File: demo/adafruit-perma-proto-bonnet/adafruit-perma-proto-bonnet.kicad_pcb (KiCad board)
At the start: 2 copper layers, 65 x 30 mm, 4 parts

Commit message: Fix bad chars in footprint identifiers
scad can't handle $ in symbol names. This will be a limitation of
the tool
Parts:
- renumbered U$1 to U1, U$3 to U3
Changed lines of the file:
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@@
 		(layer "F.Cu")
 		(at 120.953757 115.515271 -90)
-		(property "Reference" "U$1"
+		(property "Reference" "U1"
 			(at 0 0 -90)
 			(layer "F.SilkS")
@@
 		(at 175.182757 91.555271)
 		(descr "Revision Level Field - 56 mil\n\nSet version with global board attribute '>REV'")
-		(property "Reference" "U$3"
+		(property "Reference" "U3"
 			(at 0 0 0)
 			(layer "F.SilkS")

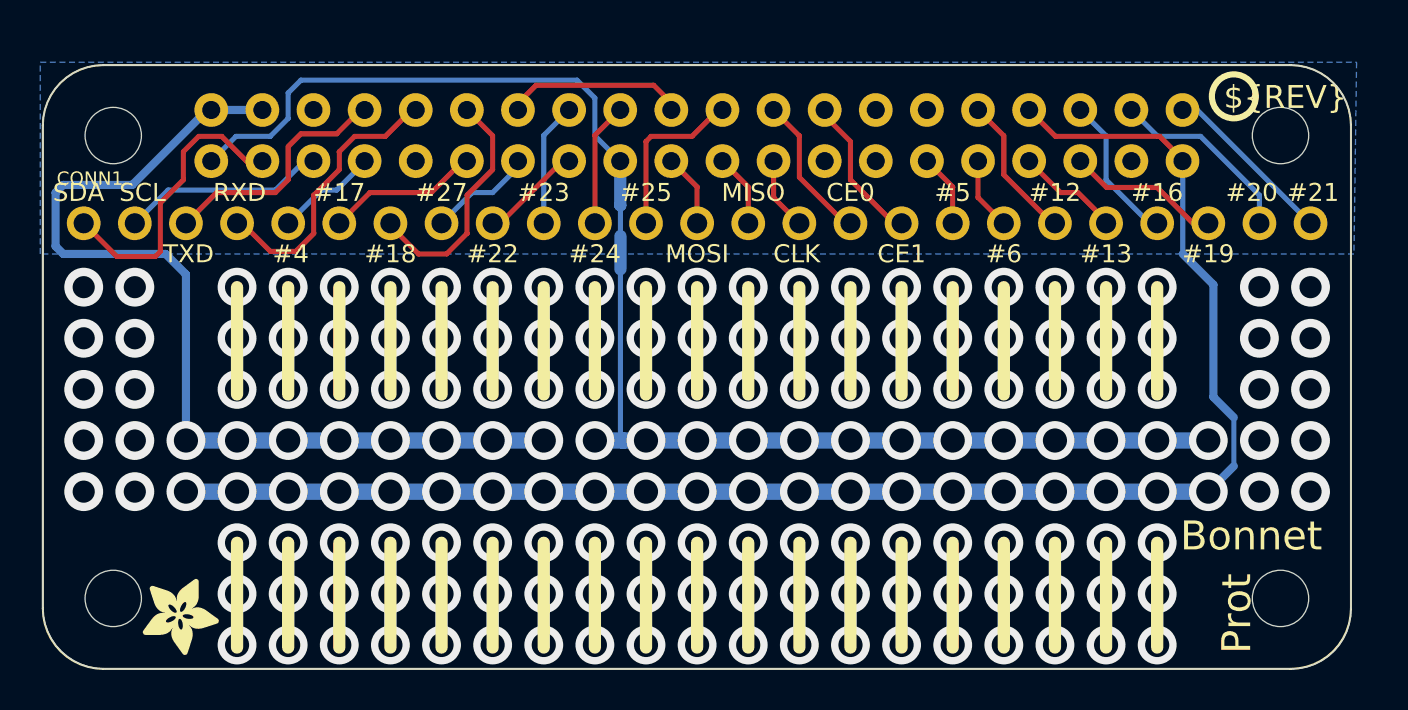
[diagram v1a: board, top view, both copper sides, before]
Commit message: Add corner mounting holes on perma proto board
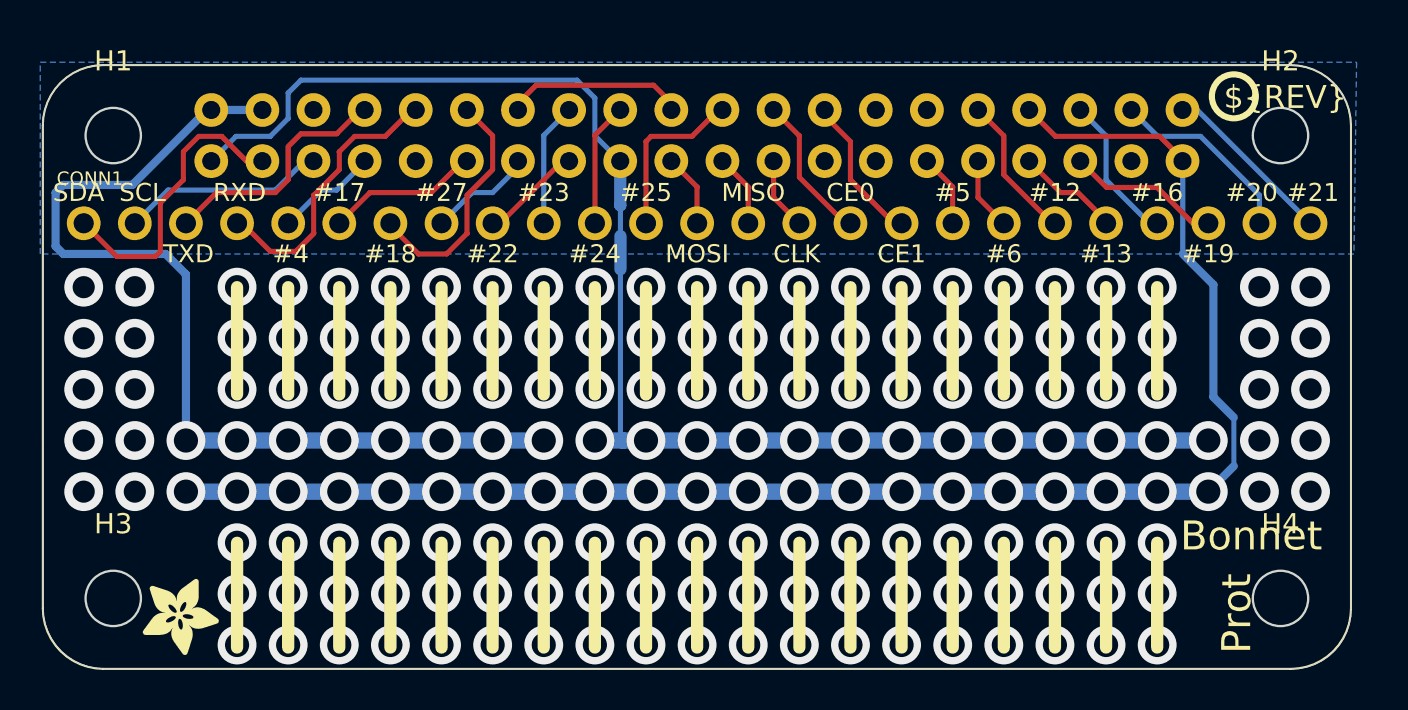
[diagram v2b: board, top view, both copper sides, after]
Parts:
- added H1: MountingHole, MountingHole:MountingHole_2.7mm_M2.5, F.Cu at (119.5, 93.5)
- added H2: MountingHole, MountingHole:MountingHole_2.7mm_M2.5, F.Cu at (177.5, 93.5)
- added H3: MountingHole, MountingHole:MountingHole_2.7mm_M2.5, F.Cu at (119.5, 116.5)
- added H4: MountingHole, MountingHole:MountingHole_2.7mm_M2.5, F.Cu at (177.5, 116.5)
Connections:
- net 3.3V renamed /3.3V
- net 5.0V renamed /5.0V
- net EECLK renamed /EECLK
- net EEDATA renamed /EEDATA
- net GPIO12 renamed /GPIO12
- net GPIO13 renamed /GPIO13
- net GPIO16 renamed /GPIO16
- net GPIO17 renamed /GPIO17
- net GPIO18 renamed /GPIO18
- net GPIO19 renamed /GPIO19
- net GPIO20 renamed /GPIO20
- net GPIO21 renamed /GPIO21
- net GPIO22 renamed /GPIO22
- net GPIO23 renamed /GPIO23
- net GPIO24 renamed /GPIO24
- net GPIO25 renamed /GPIO25
- net GPIO26 renamed /GPIO26
- net GPIO27 renamed /GPIO27
- net GPIO4 renamed /GPIO4
- net GPIO5 renamed /GPIO5
- net GPIO6 renamed /GPIO6
- net RXD renamed /RXD
- net SCL renamed /SCL
- net SDA renamed /SDA
- net SPI_CE0 renamed /SPI_CE0
- net SPI_CE1 renamed /SPI_CE1
- net SPI_MISO renamed /SPI_MISO
- net SPI_MOSI renamed /SPI_MOSI
- net SPI_SCLK renamed /SPI_SCLK
- net TXD renamed /TXD
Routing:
- net (no net): track 0.00 -> 193.0 mm, vias 0 -> 134
- net B9: track 5.08 -> 0.00 mm, vias 3 -> 0
- net B8: track 5.08 -> 0.00 mm, vias 3 -> 0
- net B7: track 5.08 -> 0.00 mm, vias 3 -> 0
- net B6: track 5.08 -> 0.00 mm, vias 3 -> 0
- net B5: track 5.08 -> 0.00 mm, vias 3 -> 0
- net B4: track 5.08 -> 0.00 mm, vias 3 -> 0
- net B3: track 5.08 -> 0.00 mm, vias 3 -> 0
- net B2: track 5.08 -> 0.00 mm, vias 3 -> 0
- net B19: track 5.08 -> 0.00 mm, vias 3 -> 0
- net B18: track 5.08 -> 0.00 mm, vias 3 -> 0
- net B17: track 5.08 -> 0.00 mm, vias 3 -> 0
- net B16: track 5.08 -> 0.00 mm, vias 3 -> 0
- net B15: track 5.08 -> 0.00 mm, vias 3 -> 0
- net B14: track 5.08 -> 0.00 mm, vias 3 -> 0
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
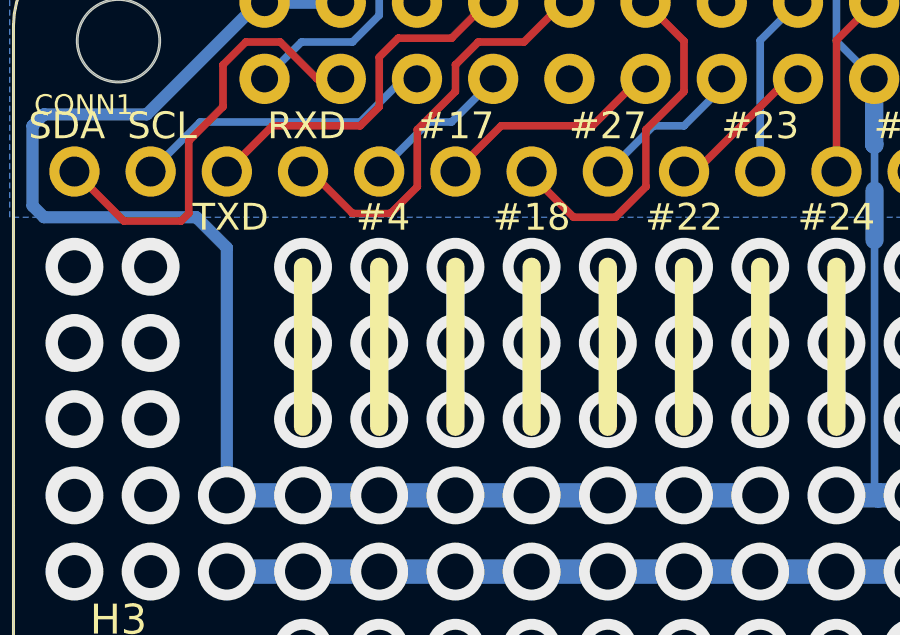
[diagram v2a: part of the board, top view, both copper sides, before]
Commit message: Add test 1206 LED and Resistor in bonnet PCB
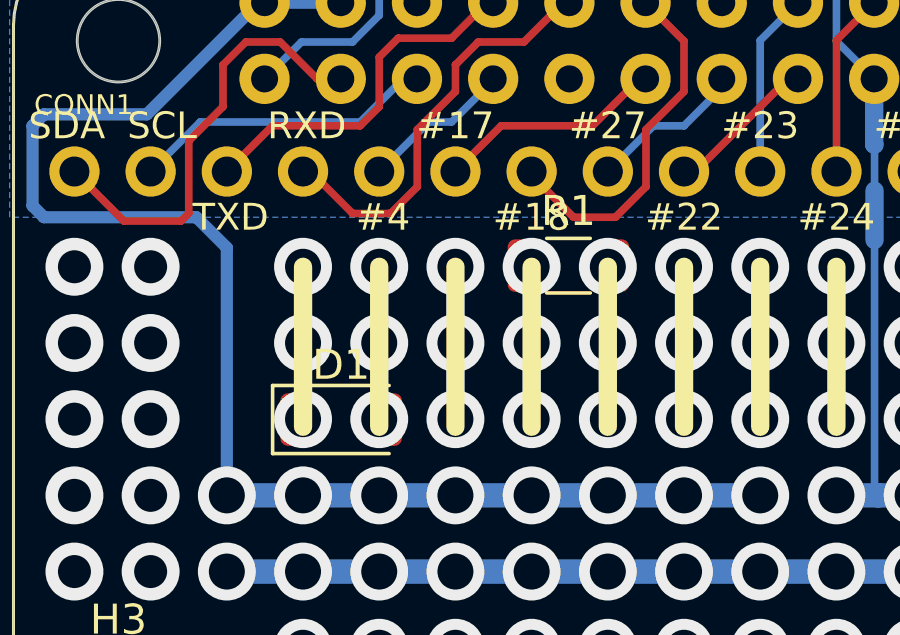
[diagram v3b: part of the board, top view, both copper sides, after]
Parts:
- added D1: IR26-21C_L110_TR8, LED_SMD:LED_1206_3216Metric, F.Cu at (126.9, 106.1)
- added R1: R, Resistor_SMD:R_1206_3216Metric, F.Cu at (134.5, 101.0)
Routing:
- net (no net): track 193.0 -> 172.7 mm, vias 134 -> 122
- net unconnected-(R1-Pad2): track 0.00 -> 5.08 mm, vias 0 -> 3
- net unconnected-(R1-Pad1): track 0.00 -> 5.08 mm, vias 0 -> 3
- net unconnected-(D1-K-Pad1): track 0.00 -> 5.08 mm, vias 0 -> 3
- net unconnected-(D1-A-Pad2): track 0.00 -> 5.08 mm, vias 0 -> 3

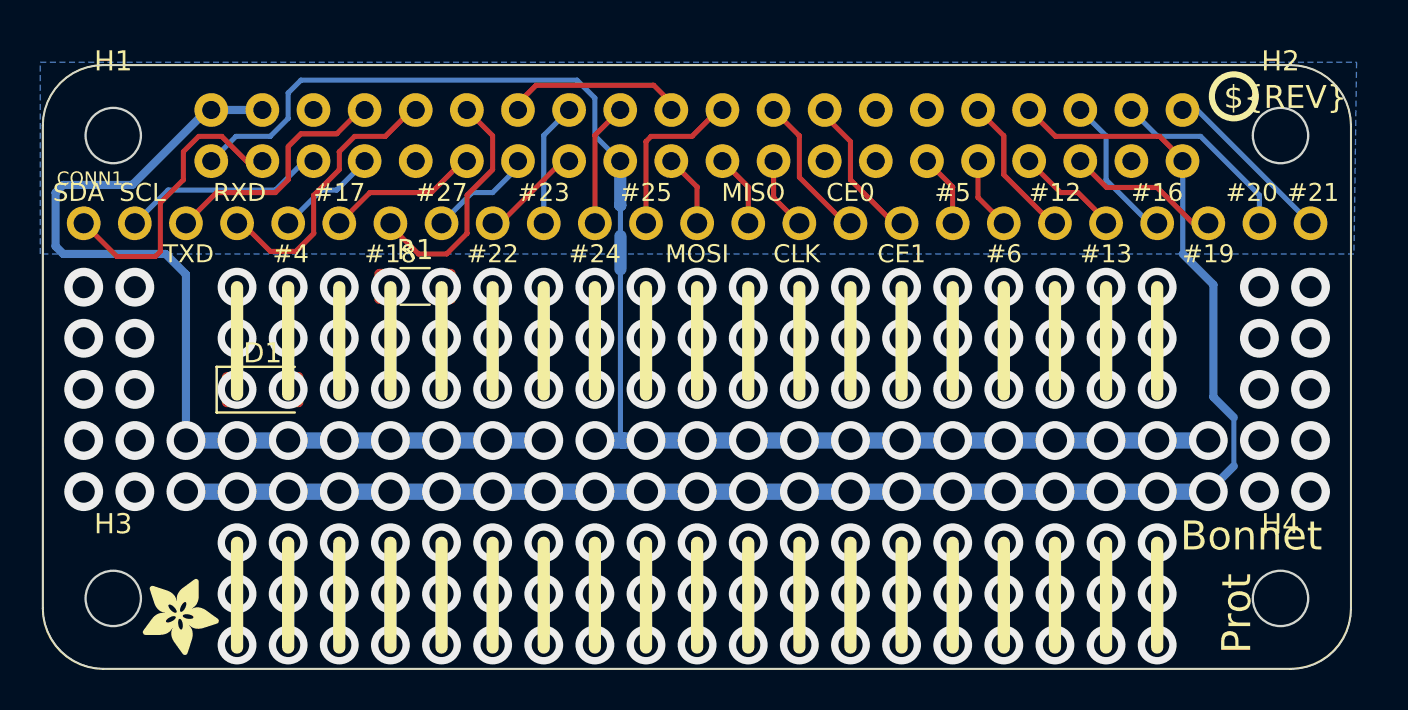
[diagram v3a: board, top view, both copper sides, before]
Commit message: Populate demo board with 9 LEDs
Location moved to lower row. Resistors are placed such that they
connect to ground. Shell gap increased slightly so that LED can
sit comfortably - probably will be loose for the resistor. Can
be tuned further.
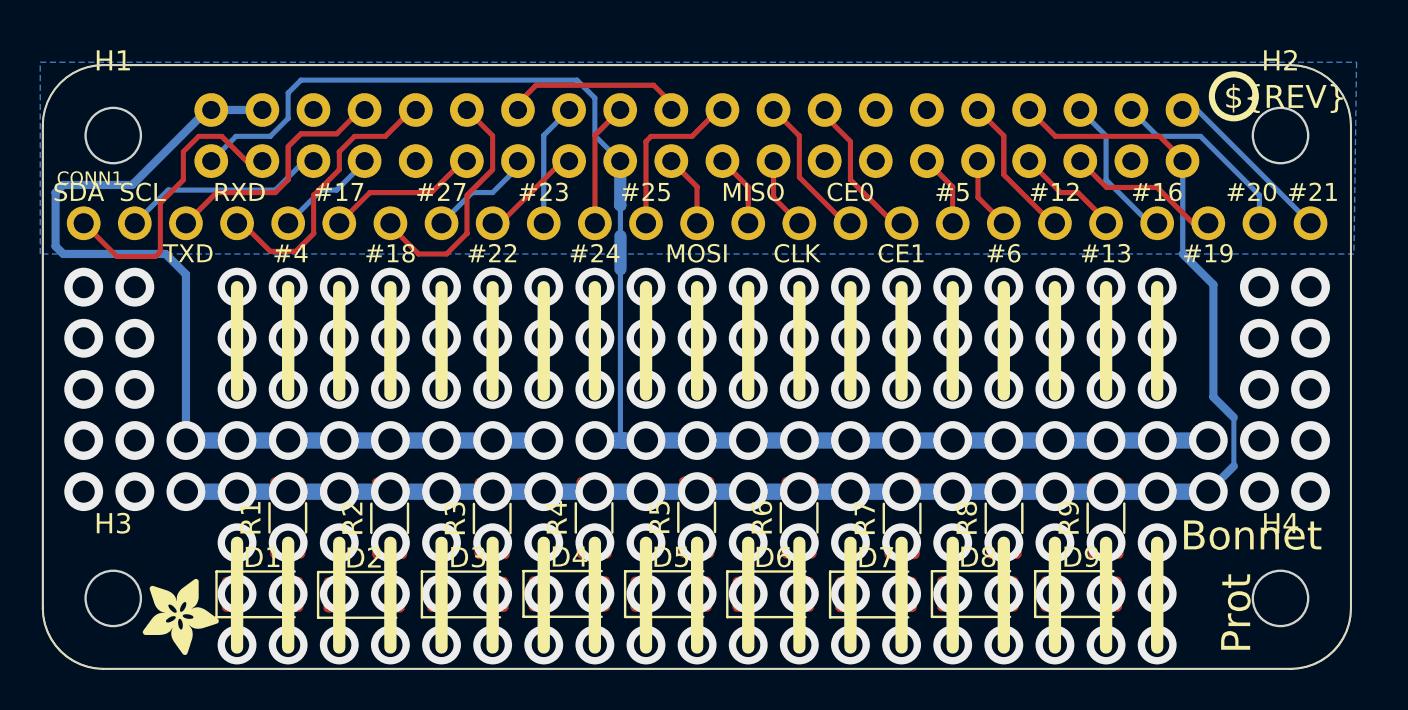
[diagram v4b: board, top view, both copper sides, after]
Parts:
- added D2: IR26-21C_L110_TR8, LED_SMD:LED_1206_3216Metric, F.Cu at (132.0, 116.3)
- added D3: IR26-21C_L110_TR8, LED_SMD:LED_1206_3216Metric, F.Cu at (137.1, 116.3)
- added D4: IR26-21C_L110_TR8, LED_SMD:LED_1206_3216Metric, F.Cu at (142.2, 116.3)
- added D5: IR26-21C_L110_TR8, LED_SMD:LED_1206_3216Metric, F.Cu at (147.2, 116.3)
- added D6: IR26-21C_L110_TR8, LED_SMD:LED_1206_3216Metric, F.Cu at (152.3, 116.3)
- added D7: IR26-21C_L110_TR8, LED_SMD:LED_1206_3216Metric, F.Cu at (157.4, 116.3)
- added D8: IR26-21C_L110_TR8, LED_SMD:LED_1206_3216Metric, F.Cu at (162.5, 116.3)
- added D9: IR26-21C_L110_TR8, LED_SMD:LED_1206_3216Metric, F.Cu at (167.6, 116.3)
- added R2: R, Resistor_SMD:R_1206_3216Metric, F.Cu at (133.2, 112.5)
- added R3: R, Resistor_SMD:R_1206_3216Metric, F.Cu at (138.3, 112.5)
- added R4: R, Resistor_SMD:R_1206_3216Metric, F.Cu at (143.4, 112.5)
- added R5: R, Resistor_SMD:R_1206_3216Metric, F.Cu at (148.5, 112.5)
- added R6: R, Resistor_SMD:R_1206_3216Metric, F.Cu at (153.6, 112.5)
- added R7: R, Resistor_SMD:R_1206_3216Metric, F.Cu at (158.7, 112.5)
- added R8: R, Resistor_SMD:R_1206_3216Metric, F.Cu at (163.8, 112.5)
- added R9: R, Resistor_SMD:R_1206_3216Metric, F.Cu at (168.8, 112.5)
- moved R1 13.1 mm to (128.2, 112.5), turned to 90 degrees
- moved D1 10.2 mm to (126.9, 116.3)
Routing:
- net (no net): track 172.7 -> 81.3 mm, vias 122 -> 68
- net unconnected-(R4-Pad1): track 0.00 -> 5.08 mm, vias 0 -> 3
- net unconnected-(D9-K-Pad1): track 0.00 -> 5.08 mm, vias 0 -> 3
- net unconnected-(D9-A-Pad2): track 0.00 -> 5.08 mm, vias 0 -> 3
- net unconnected-(D8-K-Pad1): track 0.00 -> 5.08 mm, vias 0 -> 3
- net unconnected-(D8-A-Pad2): track 0.00 -> 5.08 mm, vias 0 -> 3
- net unconnected-(D7-K-Pad1): track 0.00 -> 5.08 mm, vias 0 -> 3
- net unconnected-(D7-A-Pad2): track 0.00 -> 5.08 mm, vias 0 -> 3
- net unconnected-(D6-K-Pad1): track 0.00 -> 5.08 mm, vias 0 -> 3
- net unconnected-(D6-A-Pad2): track 0.00 -> 5.08 mm, vias 0 -> 3
- net unconnected-(D5-K-Pad1): track 0.00 -> 5.08 mm, vias 0 -> 3
- net unconnected-(D5-A-Pad2): track 0.00 -> 5.08 mm, vias 0 -> 3
- net unconnected-(D4-K-Pad1): track 0.00 -> 5.08 mm, vias 0 -> 3
- net unconnected-(D3-K-Pad1): track 0.00 -> 5.08 mm, vias 0 -> 3
- net unconnected-(D3-A-Pad2): track 0.00 -> 5.08 mm, vias 0 -> 3
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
